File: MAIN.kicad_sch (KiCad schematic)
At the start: 47 parts, among them J2 Conn_01x02_Socket, J3 Conn_01x03, J6 USB_C_Receptacle_USB2.0_16P, SW1 SW_Push, SW2 SW_Push, SW3 SW_Push, SW4 SW_Push, SW5 SW_Push, U1 USBLC6-2SC6, U2 ESP32-S3-MINI-1, U3 MP2667, U4 XC6220B331MR-G

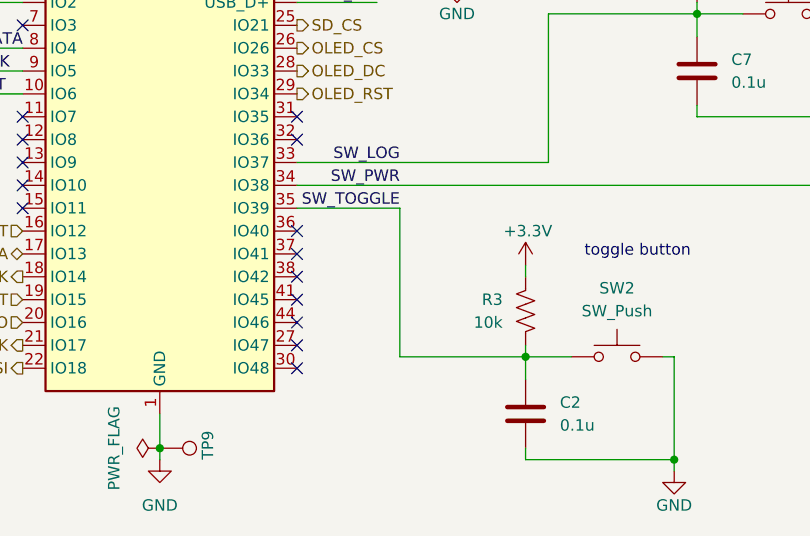
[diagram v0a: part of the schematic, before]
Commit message: changed to 8 pin connector
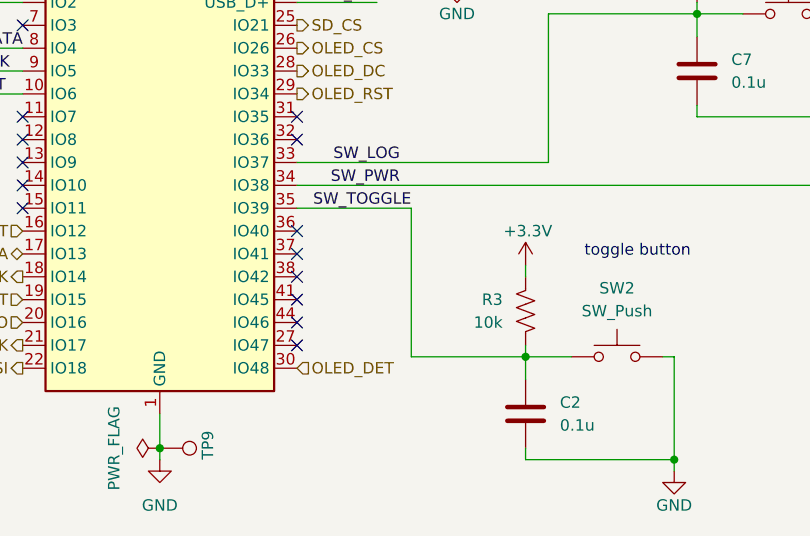
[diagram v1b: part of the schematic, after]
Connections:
- net OLED_DET: now reaches U2.30 (IO48)
- no-connect marks 18 -> 17
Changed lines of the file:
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@@
-	)
-	(no_connect
-		(at 107.95 157.48)
 	)
 	(no_connect
@@
 	(wire
 		(pts
-			(xy 107.95 139.7) (xy 119.38 139.7)
+			(xy 107.95 139.7) (xy 120.65 139.7)
 		)
 		(stroke
@@
 	(wire
 		(pts
-			(xy 119.38 139.7) (xy 119.38 156.21)
+			(xy 120.65 139.7) (xy 120.65 156.21)
 		)
 		(stroke
@@
 	(wire
 		(pts
-			(xy 119.38 156.21) (xy 133.35 156.21)
+			(xy 120.65 156.21) (xy 133.35 156.21)
 		)
 		(stroke
@@
 	)
 	(label "SW_TOGGLE"
-		(at 119.38 139.7 180)
+		(at 120.65 139.7 180)
 		(effects
 			(font
@@
 		(effects
 			(font
+				(size 1.27 1.27)
+			)
+			(justify left)
+		)
+	)
+	(hierarchical_label "OLED_DET"
+		(shape input)
+		(at 107.95 157.48 0)
+		(effects
+			(font

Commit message: REV 1.0 Ordered
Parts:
- renumbered C6 to C10, C3 to C2, C4 to C3, C5 to C4, C2 to C5, C7 to C6, C8 to C7, C9 to C8, C10 to C9, J6 to J1, J3 to J2, J2 to J3, R12 to R11, R13 to R12, R11 to R13, R4 to R3, R5 to R4, R6 to R5, R7 to R6, R8 to R7, R9 to R8, R3 to R9, SW3 to SW2, SW2 to SW3, SW5 to SW4, SW4 to SW5, TP5 to TP2, TP4 to TP3, TP9 to TP4, TP2 to TP5, TP3 to TP6, TP6 to TP7, TP7 to TP8, TP8 to TP9
